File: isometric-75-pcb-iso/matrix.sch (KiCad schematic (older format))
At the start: 252 parts

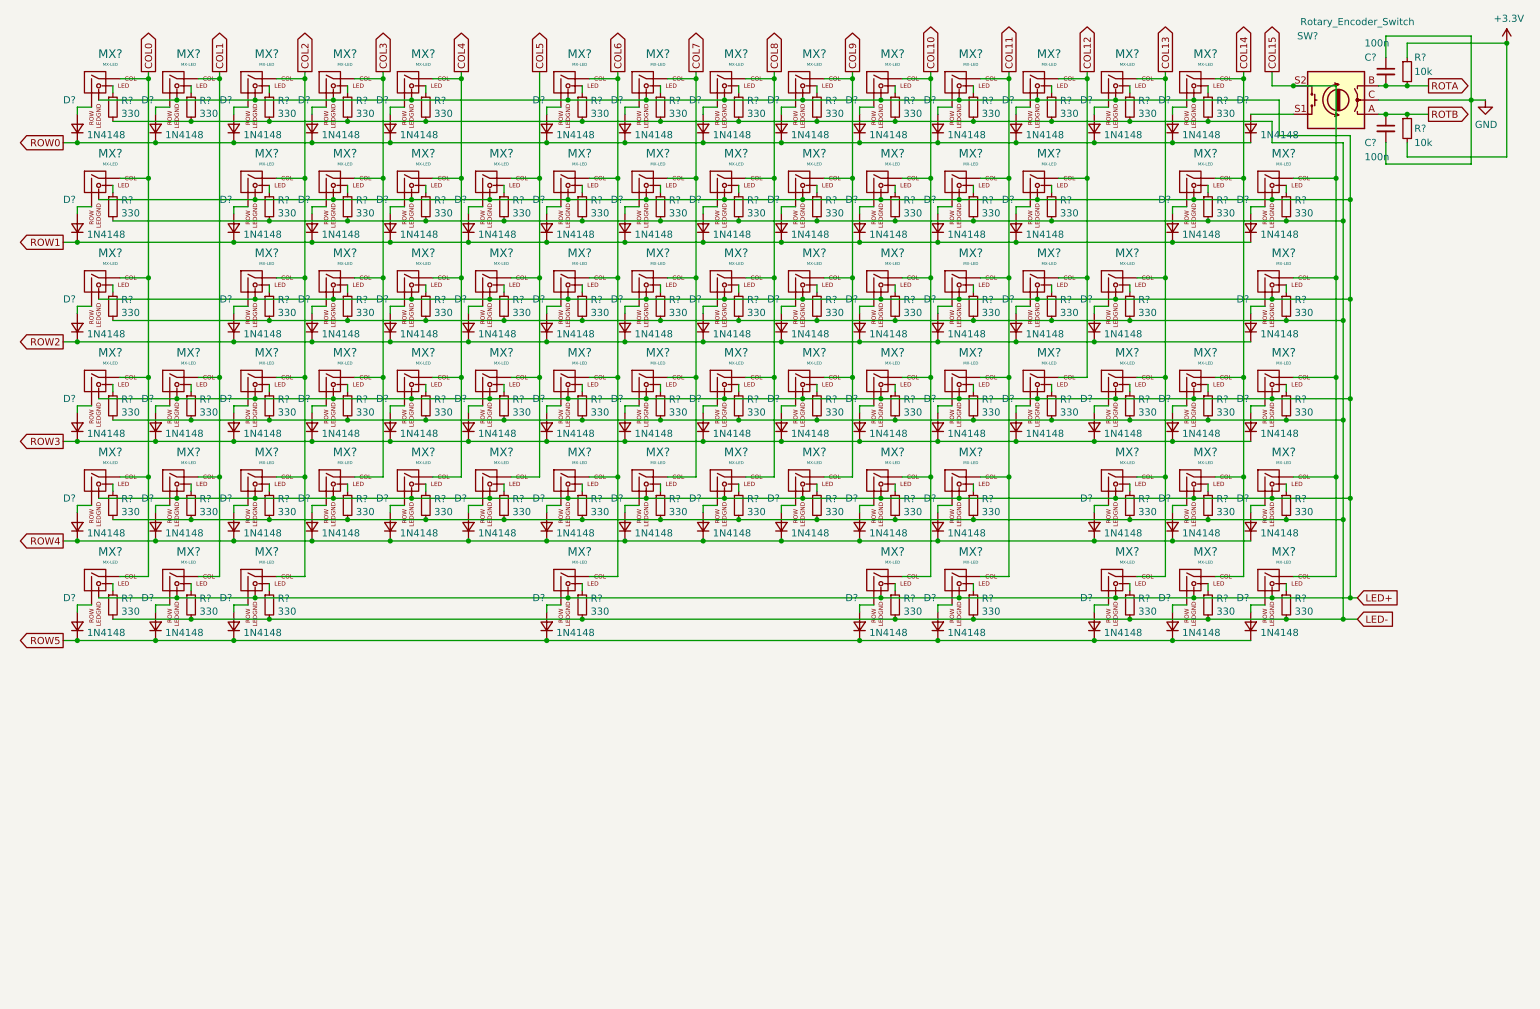
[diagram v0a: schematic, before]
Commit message: assigned footprints
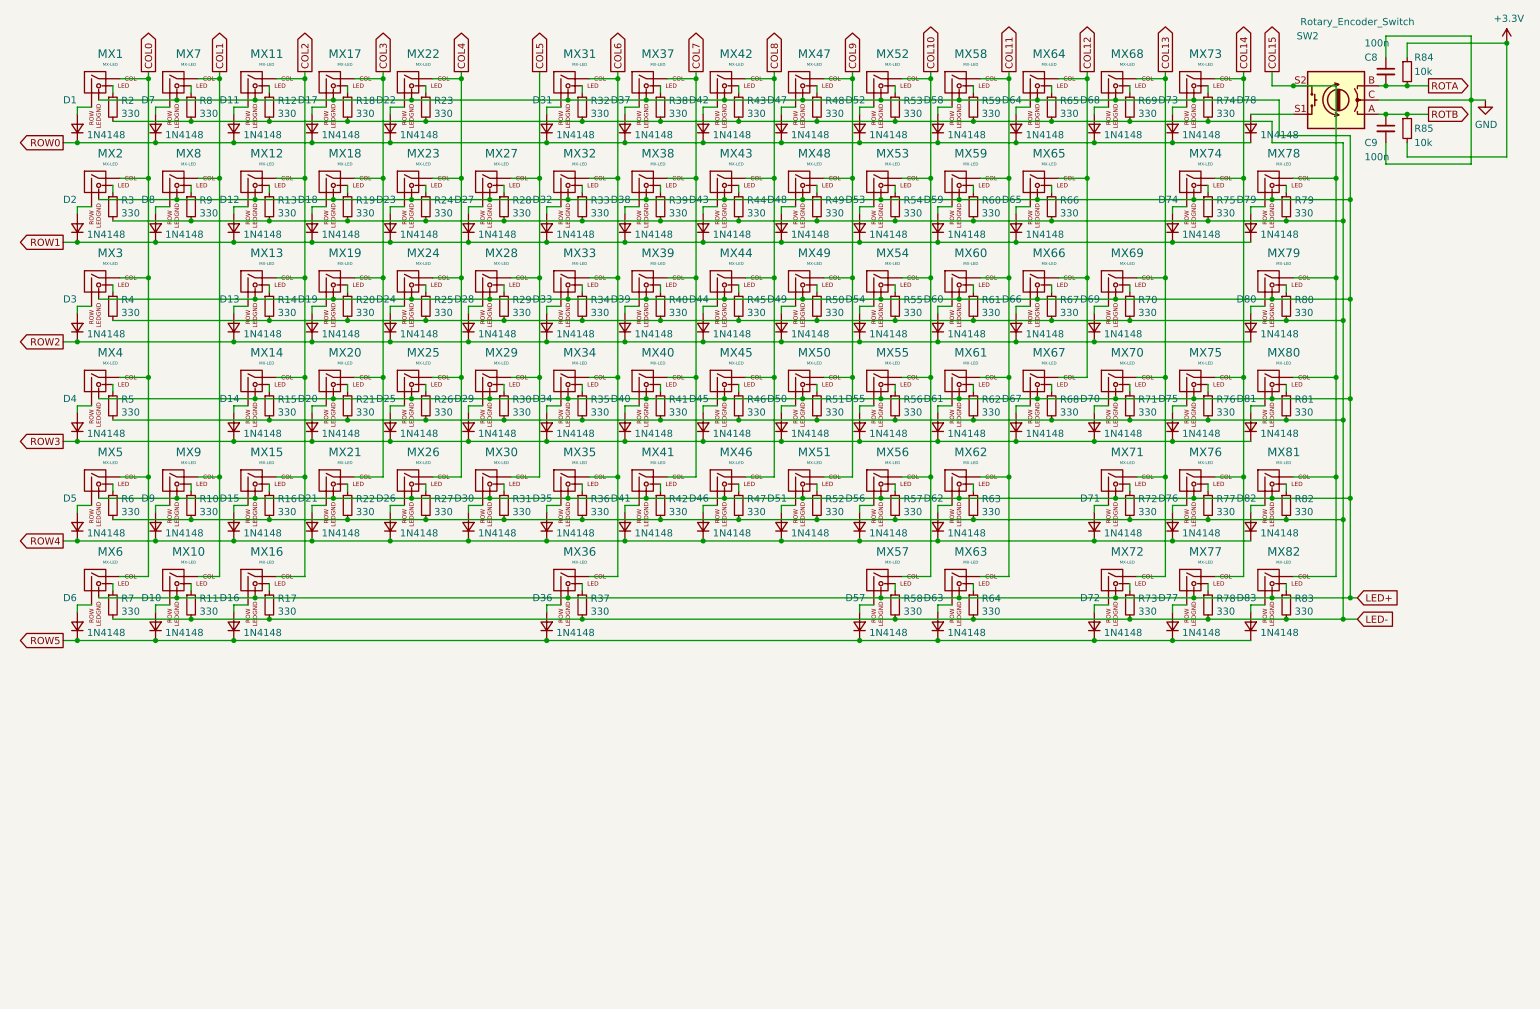
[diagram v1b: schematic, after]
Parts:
- MX1, MX11, MX12, MX13, MX14, MX15, MX2, MX22, MX23, MX24, MX25, MX26, MX27, MX28, MX29, MX30, MX31, MX32, MX33, MX34, MX35, MX37, MX38, MX39, MX40, MX41, MX42, MX43, MX44, MX45, MX46, MX47, MX48, MX49, MX50, MX51, MX52, MX53, MX54, MX55, MX56, MX58, MX59, MX60, MX61, MX62, MX64, MX65, MX66, MX67, MX68, MX69, MX7, MX70, MX72, MX73, MX76, MX77, MX78, MX79, MX8, MX80, MX81, MX82, MX9: renamed from MX?; footprint (none) -> MX_Only:MXOnly-1U
- MX10, MX16, MX17, MX18, MX19, MX20, MX21, MX5, MX6, MX63: renamed from MX?; footprint (none) -> MX_Only:MXOnly-1.25U
- MX3, MX57, MX71: renamed from MX?; footprint (none) -> MX_Only:MXOnly-1.5U
- MX36: renamed from MX?; footprint (none) -> MX_Only:MXOnly-6.25U
- MX4: renamed from MX?; footprint (none) -> MX_Only:MXOnly-1.75U
- MX74: renamed from MX?; footprint (none) -> MX_Only:MXOnly-2U-ReversedStabilizers
- MX75: renamed from MX?; footprint (none) -> MX_Only:MXOnly-ISO
- SW2: renamed from SW?; footprint (none) -> Rotary_Encoder:RotaryEncoder_Alps_EC11E-Switch_Vertical_H20mm
- gave numbers to parts that had none: 169
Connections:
- net ROW1: now also D8.1 (K)
- net ROW3: no longer D8.1 (K)
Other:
- moved on the sheet: D8, MX8, R9

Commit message: wired switches and leds
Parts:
- MX17, MX18, MX19, MX20, MX21: footprint MX_Only:MXOnly-1.25U -> MX_Only:MXOnly-1U
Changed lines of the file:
@@
 F 0 "MX17" H 2832 1324 60  0000 C CNN
 F 1 "MX-LED" H 2832 1250 20  0000 C CNN
-F 2 "MX_Only:MXOnly-1.25U" H 2125 1075 60  0001 C CNN
+F 2 "MX_Only:MXOnly-1U" H 2125 1075 60  0001 C CNN
 F 3 "" H 2125 1075 60  0001 C CNN
 	1    2750 1100
@@
 F 0 "MX18" H 2832 2024 60  0000 C CNN
 F 1 "MX-LED" H 2832 1950 20  0000 C CNN
-F 2 "MX_Only:MXOnly-1.25U" H 2125 1775 60  0001 C CNN
+F 2 "MX_Only:MXOnly-1U" H 2125 1775 60  0001 C CNN
 F 3 "" H 2125 1775 60  0001 C CNN
 	1    2750 1800
@@
 F 0 "MX19" H 2832 2724 60  0000 C CNN
 F 1 "MX-LED" H 2832 2650 20  0000 C CNN
-F 2 "MX_Only:MXOnly-1.25U" H 2125 2475 60  0001 C CNN
+F 2 "MX_Only:MXOnly-1U" H 2125 2475 60  0001 C CNN
 F 3 "" H 2125 2475 60  0001 C CNN
 	1    2750 2500
@@
 F 0 "MX20" H 2832 3424 60  0000 C CNN
 F 1 "MX-LED" H 2832 3350 20  0000 C CNN
-F 2 "MX_Only:MXOnly-1.25U" H 2125 3175 60  0001 C CNN
+F 2 "MX_Only:MXOnly-1U" H 2125 3175 60  0001 C CNN
 F 3 "" H 2125 3175 60  0001 C CNN
 	1    2750 3200
@@
 F 0 "MX21" H 2832 4124 60  0000 C CNN
 F 1 "MX-LED" H 2832 4050 20  0000 C CNN
-F 2 "MX_Only:MXOnly-1.25U" H 2125 3875 60  0001 C CNN
+F 2 "MX_Only:MXOnly-1U" H 2125 3875 60  0001 C CNN
 F 3 "" H 2125 3875 60  0001 C CNN
 	1    2750 3900

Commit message: continued the pcb
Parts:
- renumbered C8 to C201, C9 to C202, D1 to D201, D2 to D202, D3 to D203, D4 to D204, D5 to D205, D6 to D206, D7 to D207, D8 to D208, D9 to D209, D10 to D210, D11 to D211, D12 to D212, D13 to D213, D14 to D214, D15 to D215, D16 to D216, D17 to D217, D18 to D218, D19 to D219, D20 to D220, D21 to D221, D22 to D222, D23 to D223, D24 to D224, D25 to D225, D26 to D226, D27 to D227, D28 to D228, D29 to D229, D30 to D230, D31 to D231, D32 to D232, D33 to D233, D34 to D234, D35 to D235, D36 to D236, D37 to D237, D38 to D238, D39 to D239, D40 to D240, D41 to D241, D42 to D242, D43 to D243, D44 to D244, D45 to D245, D46 to D246, D47 to D247, D48 to D248, D49 to D249, D50 to D250, D51 to D251, D52 to D252, D53 to D253, D54 to D254, D55 to D255, D56 to D256, D57 to D257, D58 to D258, D59 to D259, D60 to D260, D61 to D261, D62 to D262, D63 to D263, D64 to D264, D65 to D265, D66 to D266, D67 to D267, D68 to D268, D69 to D269, D70 to D270, D71 to D271, D72 to D272, D73 to D273, D74 to D274, D75 to D275, D76 to D276, D77 to D277, D78 to D278, D79 to D279, D80 to D280, D81 to D281, D82 to D282, D83 to D283, MX1 to MX201, MX2 to MX202, MX3 to MX203, MX4 to MX204, MX5 to MX205, MX6 to MX206, MX7 to MX207, MX8 to MX208, MX9 to MX209, MX10 to MX210, MX11 to MX211, MX12 to MX212, MX13 to MX213, MX14 to MX214, MX15 to MX215, MX16 to MX216, MX17 to MX217, MX18 to MX218, MX19 to MX219, MX20 to MX220, MX21 to MX221, MX22 to MX222, MX23 to MX223, MX24 to MX224, MX25 to MX225, MX26 to MX226, MX27 to MX227, MX28 to MX228, MX29 to MX229, MX30 to MX230, MX31 to MX231, MX32 to MX232, MX33 to MX233, MX34 to MX234, MX35 to MX235, MX36 to MX236, MX37 to MX237, MX38 to MX238, MX39 to MX239, MX40 to MX240, MX41 to MX241, MX42 to MX242, MX43 to MX243, MX44 to MX244, MX45 to MX245, MX46 to MX246, MX47 to MX247, MX48 to MX248, MX49 to MX249, MX50 to MX250, MX51 to MX251, MX52 to MX252, MX53 to MX253, MX54 to MX254, MX55 to MX255, MX56 to MX256, MX57 to MX257, MX58 to MX258, MX59 to MX259, MX60 to MX260, MX61 to MX261, MX62 to MX262, MX63 to MX263, MX64 to MX264, MX65 to MX265, MX66 to MX266, MX67 to MX267, MX68 to MX268, MX69 to MX269, MX70 to MX270, MX71 to MX271, MX72 to MX272, MX73 to MX273, MX74 to MX274, MX75 to MX275, MX76 to MX276, MX77 to MX277, MX78 to MX278, MX79 to MX279, MX80 to MX280, MX81 to MX281, MX82 to MX282, R2 to R201, R3 to R202, R4 to R203, R5 to R204, R6 to R205, R7 to R206, R8 to R207, R9 to R208, R10 to R209, R11 to R210, R12 to R211, R13 to R212, R14 to R213, R15 to R214, R16 to R215, R17 to R216, R18 to R217, R19 to R218, R20 to R219, R21 to R220, R22 to R221, R23 to R222, R24 to R223, R25 to R224, R26 to R225, R27 to R226, R28 to R227, R29 to R228, R30 to R229, R31 to R230, R32 to R231, R33 to R232, R34 to R233, R35 to R234, R36 to R235, R37 to R236, R38 to R237, R39 to R238, R40 to R239, R41 to R240, R42 to R241, R43 to R242, R44 to R243, R45 to R244, R46 to R245, R47 to R246, R48 to R247, R49 to R248, R50 to R249, R51 to R250, R52 to R251, R53 to R252, R54 to R253, R55 to R254, R56 to R255, R57 to R256, R58 to R257, R59 to R258, R60 to R259, R61 to R260, R62 to R261, R63 to R262, R64 to R263, R65 to R264, R66 to R265, R67 to R266, R68 to R267, R69 to R268, R70 to R269, R71 to R270, R72 to R271, R73 to R272, R74 to R273, R75 to R274, R76 to R275, R77 to R276, R78 to R277, R79 to R278, R80 to R279, R81 to R280, R82 to R281, R83 to R282, R84 to R283, R85 to R284, SW2 to SW201

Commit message: more pcb wiring
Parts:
- R201, R202, R203, R204, R205, R206, R207, R208, R209, R210, R211, R212, R213, R214, R215, R216, R217, R218, R219, R220, R221, R222, R223, R224, R225, R226, R227, R228, R229, R230, R231, R232, R233, R234, R235, R236, R237, R238, R239, R240, R241, R242, R243, R244, R245, R246, R247, R248, R249, R250, R251, R252, R253, R254, R255, R256, R257, R258, R259, R260, R261, R262, R263, R264, R265, R266, R267, R268, R269, R270, R271, R272, R273, R274, R275, R276, R277, R278, R279, R280, R281, R282, R283, R284: footprint Resistor_SMD:R_0402_1005Metric -> Resistor_SMD:R_0603_1608Metric

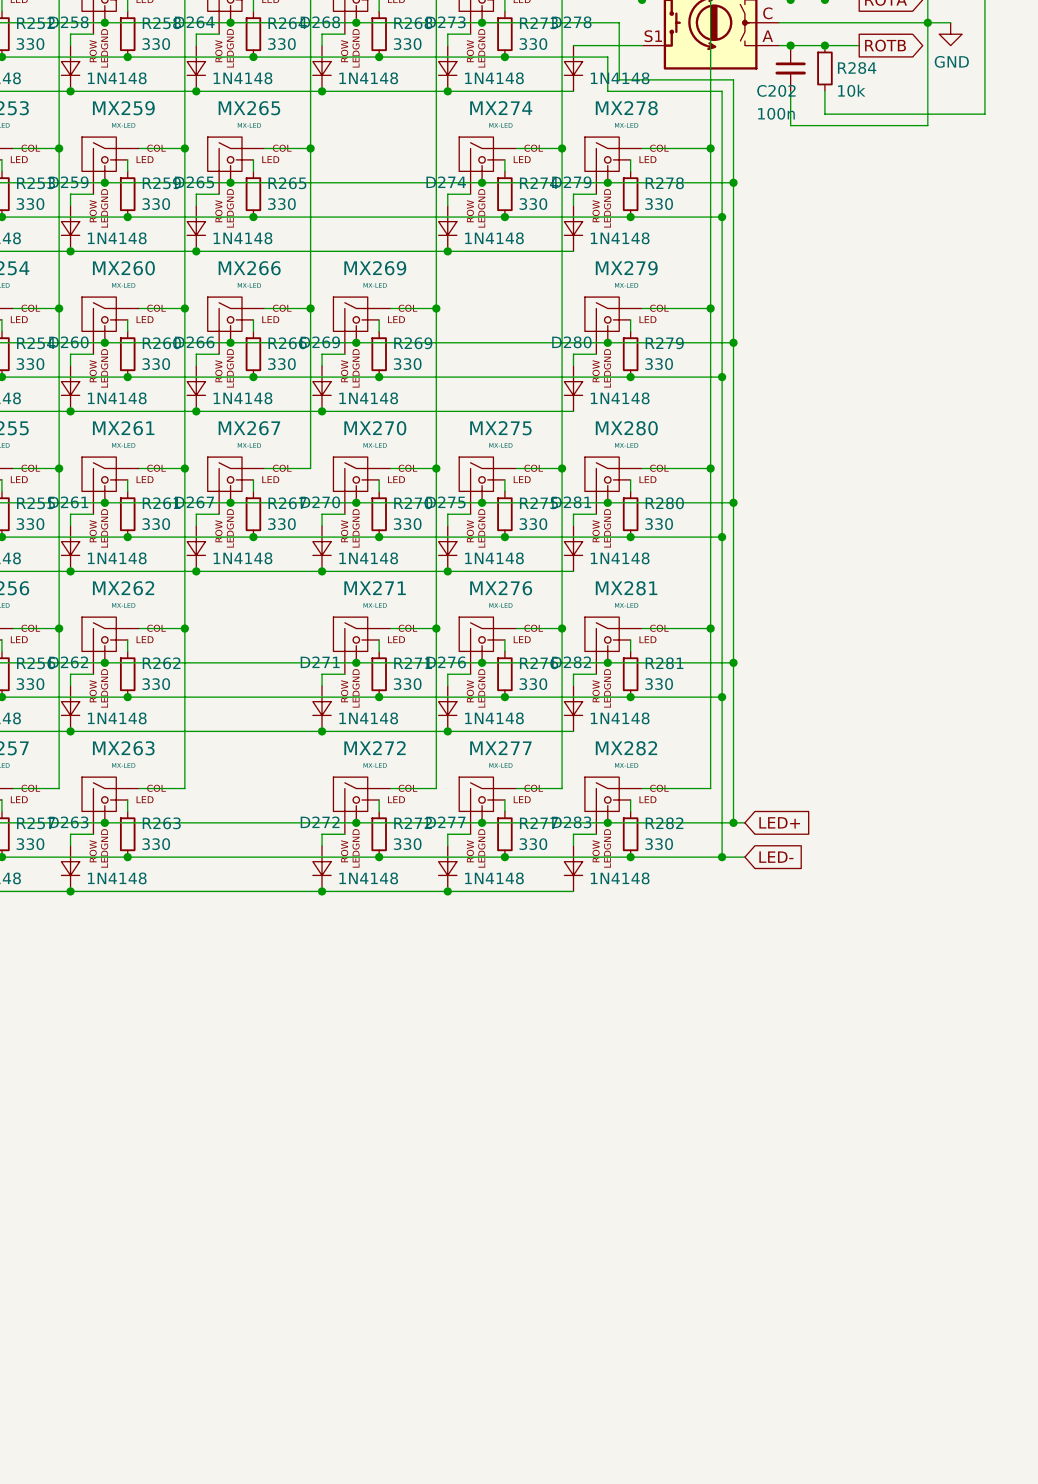
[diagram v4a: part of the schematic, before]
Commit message: finished wiring cols, changed jlc connector color
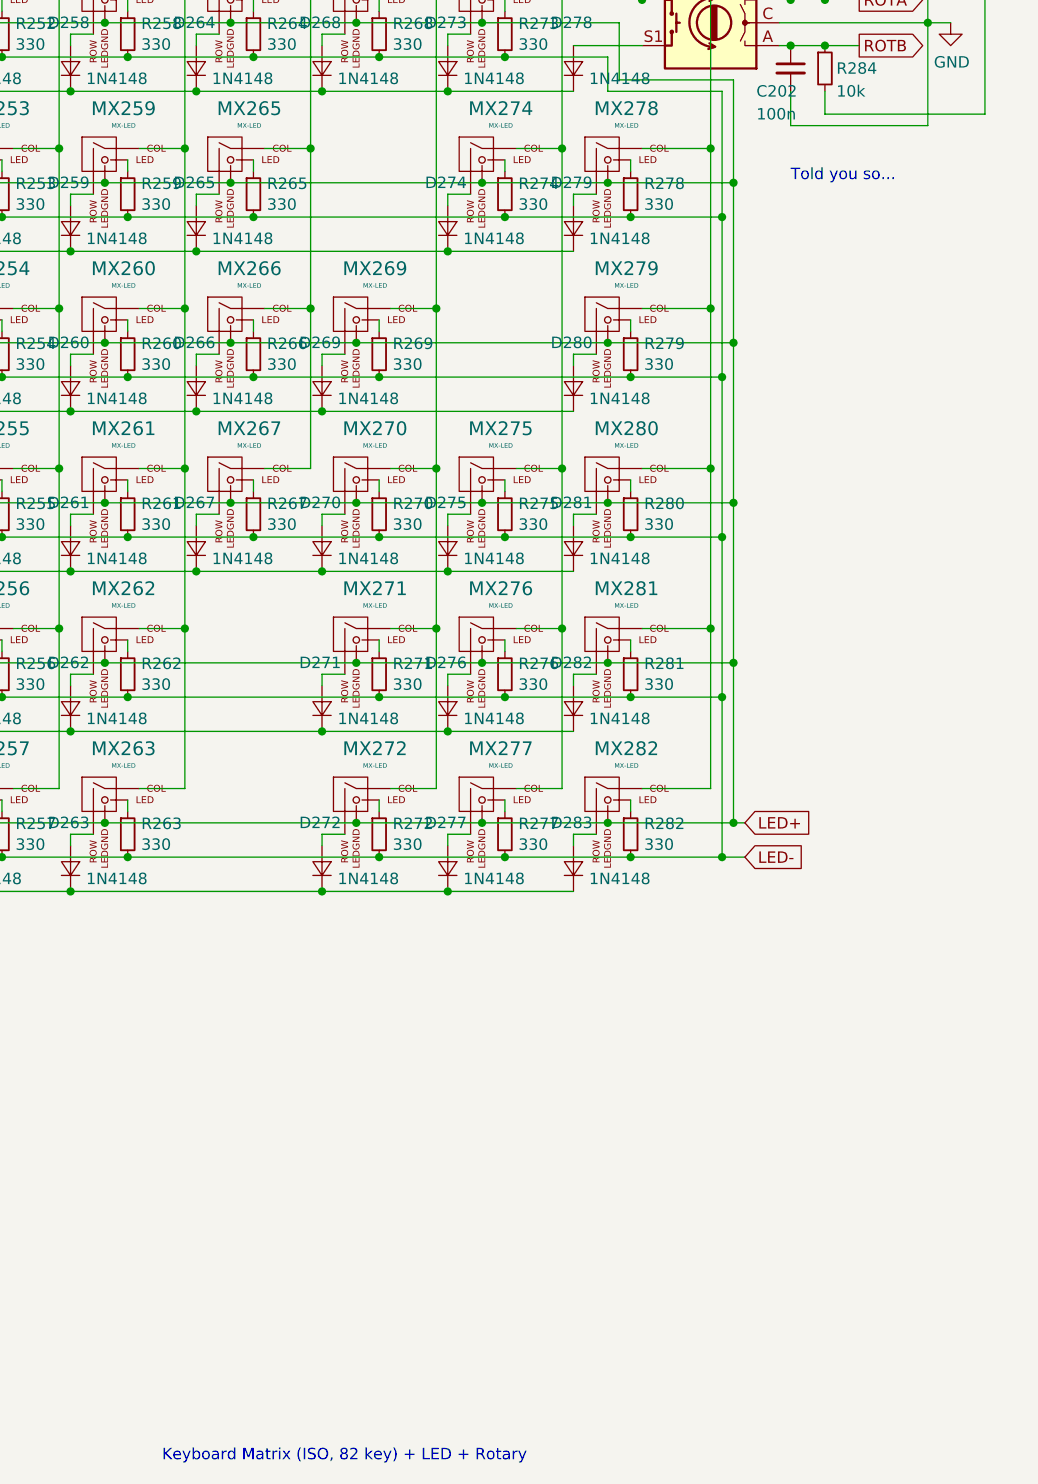
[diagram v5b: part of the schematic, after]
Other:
- note added: "Keyboard Matrix (ISO, 82 key) + LED + Rotary"
- note added: "Told you so..."
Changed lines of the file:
@@
 Wire Wire Line
 	1950 1750 1950 3850
+Text Notes 10150 1900 0    50   ~ 0
+Told you so...
+Text Notes 7400 7500 0    50   ~ 0
+Keyboard Matrix (ISO, 82 key) + LED + Rotary
 $EndSCHEMATC
